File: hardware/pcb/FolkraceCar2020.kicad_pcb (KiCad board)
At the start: 2 copper layers, 3 parts, among them J2 Jetson Nano Header, U1 TPS25940x-Q1, U2 OKL-T_6-W12N-C

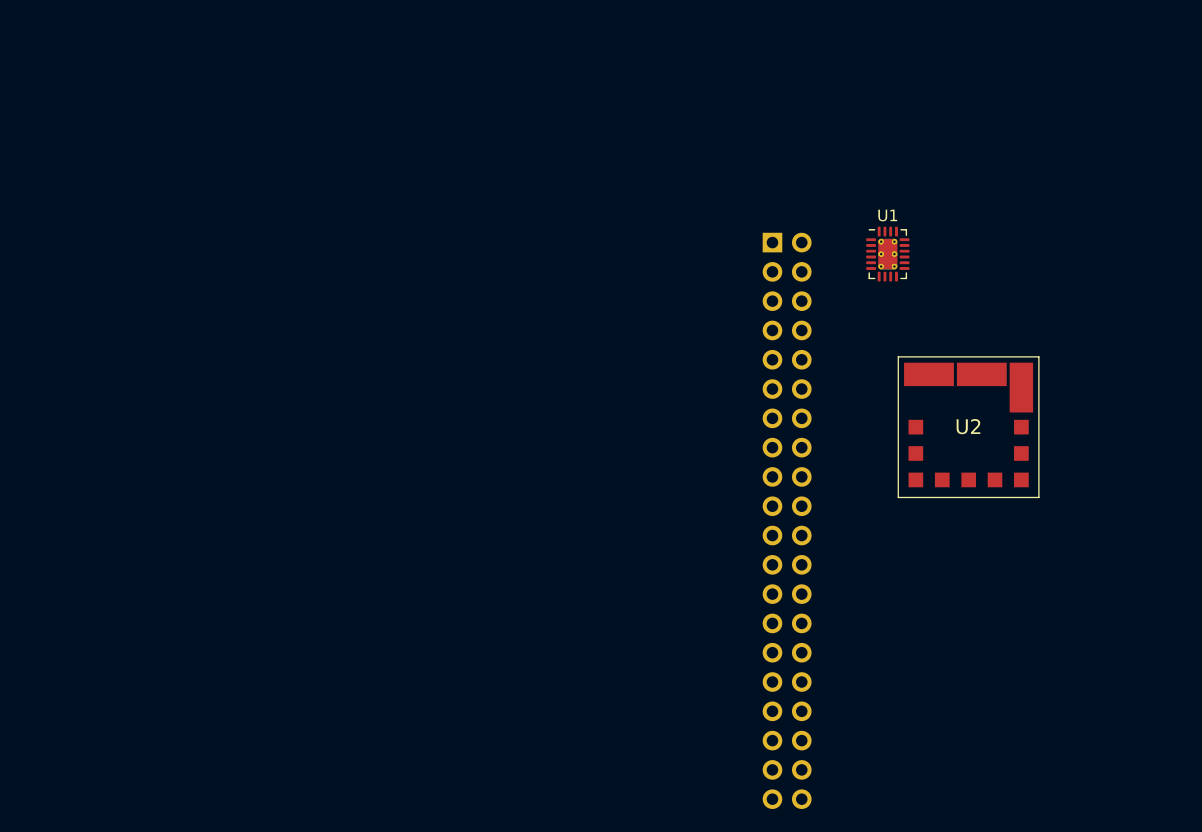
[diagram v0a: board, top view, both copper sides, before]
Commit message: Outline added to pcb layout
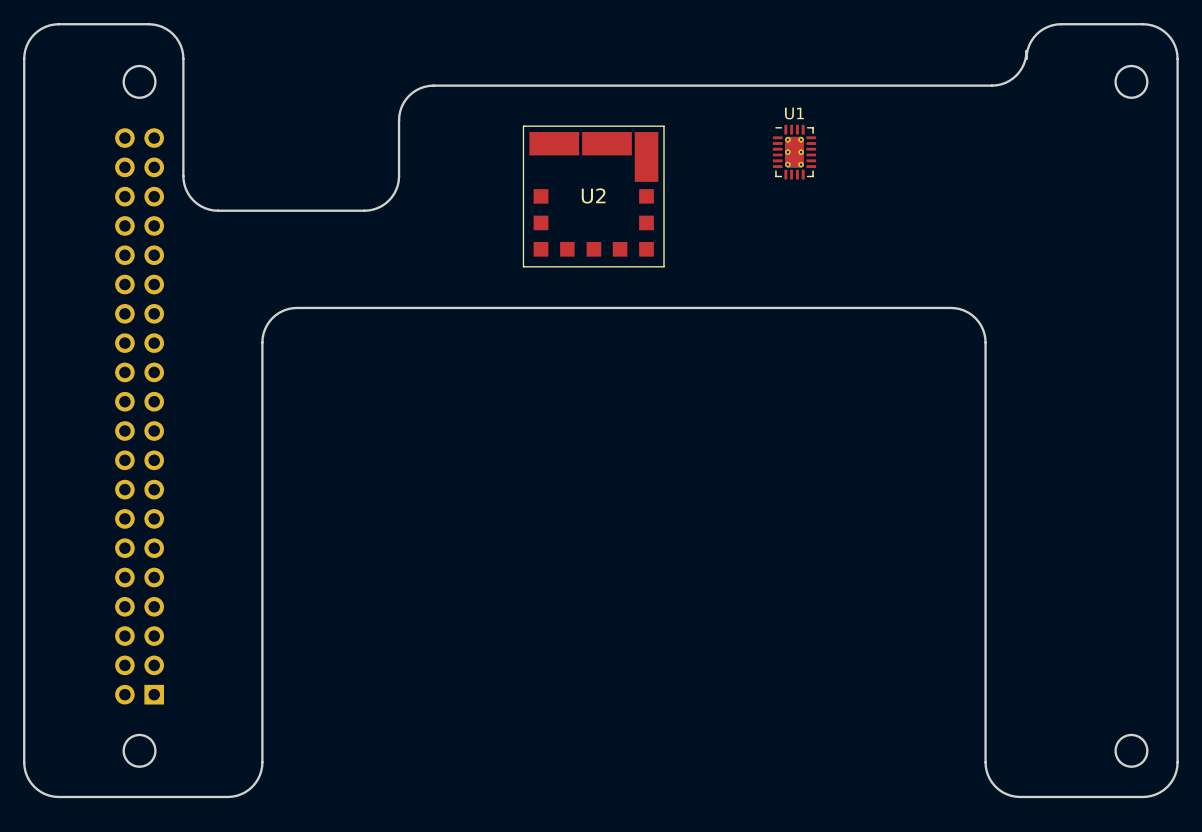
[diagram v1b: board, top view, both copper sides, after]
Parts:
- moved J2 66.4 mm to (86.4, 134.2), turned to 0 degrees
- moved U2 38.2 mm to (124.5, 91.0)
- moved U1 12.0 mm to (141.9, 87.2)
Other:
- board outline added: 100 x 67 mm

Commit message: updated schematic
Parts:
- added D1: LED RED, LED_SMD:LED_0603_1608Metric, F.Cu at (162.5, 87.0)
- added D2: LED GREEN, LED_SMD:LED_0603_1608Metric, F.Cu at (157.5, 92.2)
- added R1: R, Resistor_SMD:R_0603_1608Metric, F.Cu at (150.5, 96.8)
- added R2: R, Resistor_SMD:R_0603_1608Metric, F.Cu at (162.5, 89.5)
- added R3: R, Resistor_SMD:R_0603_1608Metric, F.Cu at (154.5, 96.8)
- added R4: R, Resistor_SMD:R_0603_1608Metric, F.Cu at (166.5, 87.0)
- added R5: R, Resistor_SMD:R_0603_1608Metric, F.Cu at (161.5, 92.1)
- added R6: R, Resistor_SMD:R_0603_1608Metric, F.Cu at (166.5, 89.5)
- added R8: R, Resistor_SMD:R_0603_1608Metric, F.Cu at (158.5, 94.7)
- added SW1: SPST, Button_Switch_SMD:SW_DIP_SPSTx01_Slide_Omron_A6S-110x_W8.9mm_P2.54mm, F.Cu at (154.5, 88.3)
- added U3: ADS1115IDGS, Package_SO:TSSOP-10_3x3mm_P0.5mm, F.Cu at (152.0, 93.2)
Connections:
- U1 pad 16: Net-(U1-Pad16) -> GND
- U1 pad 2: Net-(U1-Pad2) -> Net-(R8-Pad1)
- U1 pad 21: Net-(U1-Pad21) -> GND
- U1 pad 3: Net-(U1-Pad3) -> VBUS
- U1 pad 4: Net-(U1-Pad4) -> VBUS
- U1 pad 5: Net-(U1-Pad5) -> VBUS
- U1 pad 6: Net-(U1-Pad6) -> VBUS
- U1 pad 7: Net-(U1-Pad7) -> VBUS
- U1 pad 8: Net-(U1-Pad8) -> VBUS
- U2 pad 1: Net-(U2-Pad1) -> Net-(R8-Pad1)
- U2 pad 2: Net-(U2-Pad2) -> VBUS

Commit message: added todo in schematic
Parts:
- added D3: LED GREEN, LED_SMD:LED_0603_1608Metric, F.Cu at (127.4, 74.3)
- added J3: Conn_01x03_Male, Connector_JST:JST_PH_B3B-PH-K_1x03_P2.00mm_Vertical, F.Cu at (110.5, 75.7)
- added J4: Conn_01x02_Male, Connector_JST:JST_PH_B2B-PH-K_1x02_P2.00mm_Vertical, F.Cu at (120.4, 75.7)
- added Q1: BSS138, Package_TO_SOT_SMD:SOT-23, F.Cu at (109.7, 81.8)
- added Q2: DMN10H220L, Package_TO_SOT_SMD:SOT-23, F.Cu at (114.2, 81.8)
- added R10: R, Resistor_SMD:R_0603_1608Metric, F.Cu at (118.4, 83.3)
- added R11: R, Resistor_SMD:R_0603_1608Metric, F.Cu at (127.4, 79.4)
- added R12: R, Resistor_SMD:R_0603_1608Metric, F.Cu at (122.4, 83.3)
- added R7: R, Resistor_SMD:R_0603_1608Metric, F.Cu at (127.4, 76.8)
- added R9: 1.3k, Resistor_SMD:R_0603_1608Metric, F.Cu at (122.4, 80.8)
- R5: value R -> 0
- moved R5 44.6 mm to (118.4, 80.8)
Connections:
- R5 pad 1: Net-(R4-Pad1) -> Net-(R5-Pad1)
- R5 pad 2: GND -> Net-(Q1-Pad3)
- R8 pad 1: Net-(R8-Pad1) -> Net-(Q1-Pad1)
- U1 pad 19: Net-(R7-Pad1) -> /IMON
- U1 pad 2: Net-(R8-Pad1) -> Net-(Q1-Pad1)
- U2 pad 1: Net-(R8-Pad1) -> Net-(R5-Pad1)
- U2 pad 3: Net-(U2-Pad3) -> GND
- U2 pad 4: Net-(U2-Pad4) -> +5V
- U2 pad 5: Net-(U2-Pad5) -> +5V
- U2 pad 7: Net-(U2-Pad7) -> GND
- U3 pad 3: Net-(U3-Pad3) -> GND
- U3 pad 4: Net-(U3-Pad4) -> /VMON
- U3 pad 5: Net-(U3-Pad5) -> /IMON

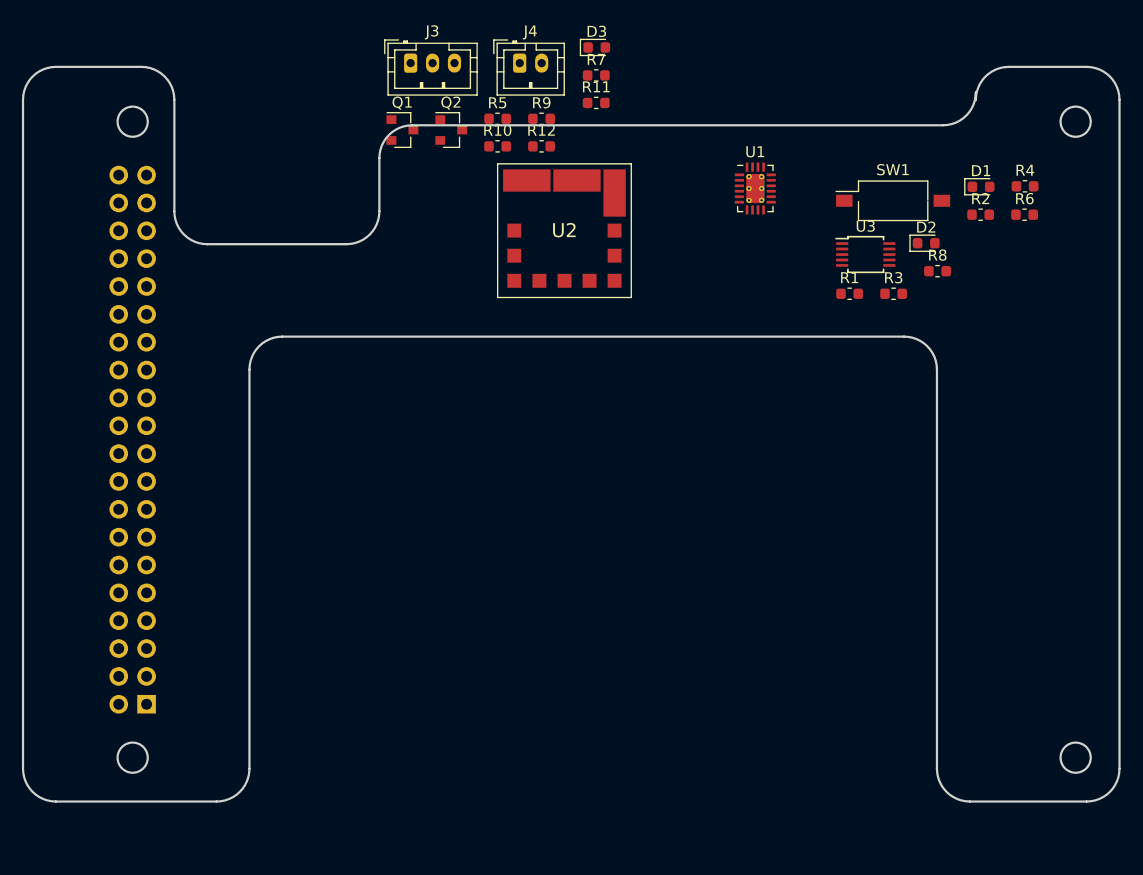
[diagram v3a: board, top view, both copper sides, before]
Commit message: added new outline and RP connector
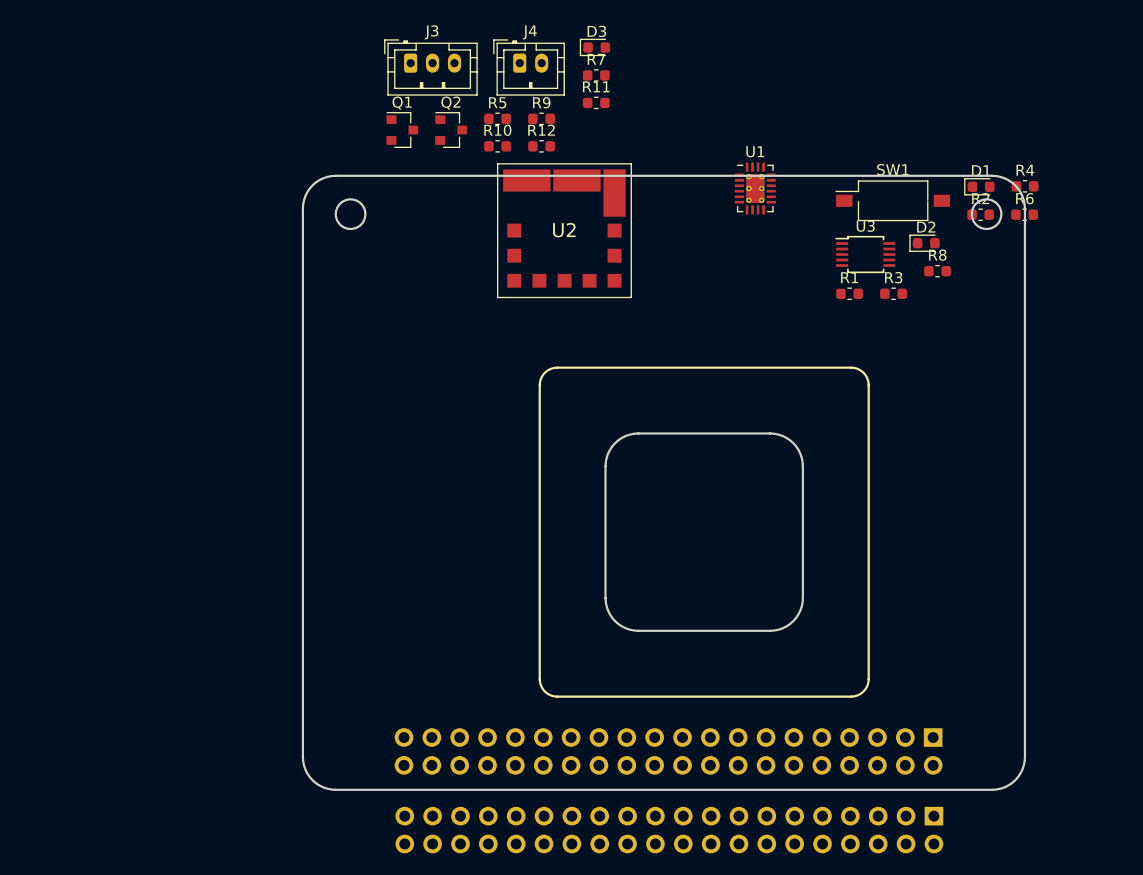
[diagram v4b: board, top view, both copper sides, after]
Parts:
- added J5: Raspberry_Pi_2_3, Connector_PinSocket_2.54mm:PinSocket_2x20_P2.54mm_Vertical, B.Cu at (158.2, 144.4)
- moved J2 71.8 mm to (158.1, 137.2), turned to 90 degrees
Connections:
- J2 pad 10: /UART_2_RX -> (no net)
- J2 pad 11: /UART_2_RTS -> (no net)
- J2 pad 12: /I2S_4_SCLK -> (no net)
- J2 pad 13: /SPI_2_SCK -> (no net)
- J2 pad 15: /LCD_TE -> (no net)
- J2 pad 16: /SPI_2_CS1 -> (no net)
- J2 pad 18: /SPI_2_CS0 -> (no net)
- J2 pad 19: /SPI_1_MOSI -> (no net)
- J2 pad 21: /SPI_1_MISO -> (no net)
- J2 pad 22: /SPI_2_MISO -> (no net)
- J2 pad 23: /SPI_1_SCK -> (no net)
- J2 pad 24: /SPI_1_CS0 -> (no net)
- J2 pad 26: /SPI_1_CS1 -> (no net)
- J2 pad 27: /I2C_1_SDA -> (no net)
- J2 pad 28: /I2C_1_SCL -> (no net)
- J2 pad 29: /CAM_AF_EN -> (no net)
- J2 pad 3: /I2C_2SDA -> (no net)
- J2 pad 31: /GPIO_PZ0 -> (no net)
- J2 pad 32: /LCD_BL_PWM -> (no net)
- J2 pad 33: /GPIO_PE6 -> (no net)
- J2 pad 35: /I2S_4_LRCK -> (no net)
- J2 pad 36: /UART_2_CTS -> (no net)
- J2 pad 37: /SPI_2_MOSI -> (no net)
- J2 pad 38: /I2S_4_SDIN -> (no net)
- J2 pad 40: /I2S_4_SDOUT -> (no net)
- J2 pad 5: /I2C_2_SCL -> (no net)
- J2 pad 7: /AUDIO_MCLK -> (no net)
- J2 pad 8: /UART_2_TX -> (no net)
- J3 pad 2: /SERVO_PWM -> (no net)
- Q2 pad 1: /FAN_CTRL -> (no net)
- U1 pad 1: Net-(U1-Pad1) -> (no net)
- U1 pad 18: Net-(C3-Pad1) -> (no net)
- U2 pad 11: Net-(U2-Pad11) -> (no net)
- U2 pad 12: Net-(U2-Pad12) -> (no net)
- U2 pad 8: Net-(U2-Pad8) -> (no net)
- U2 pad 9: Net-(U2-Pad9) -> (no net)
- U3 pad 1: Net-(U3-Pad1) -> (no net)
- U3 pad 10: Net-(U3-Pad10) -> (no net)
- U3 pad 2: Net-(U3-Pad2) -> (no net)
- U3 pad 6: Net-(U3-Pad6) -> (no net)
- U3 pad 7: Net-(U3-Pad7) -> (no net)
- U3 pad 8: Net-(C4-Pad1) -> (no net)
- U3 pad 9: Net-(U3-Pad9) -> (no net)
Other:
- board size 100 x 67 mm -> 65.8 x 56 mm

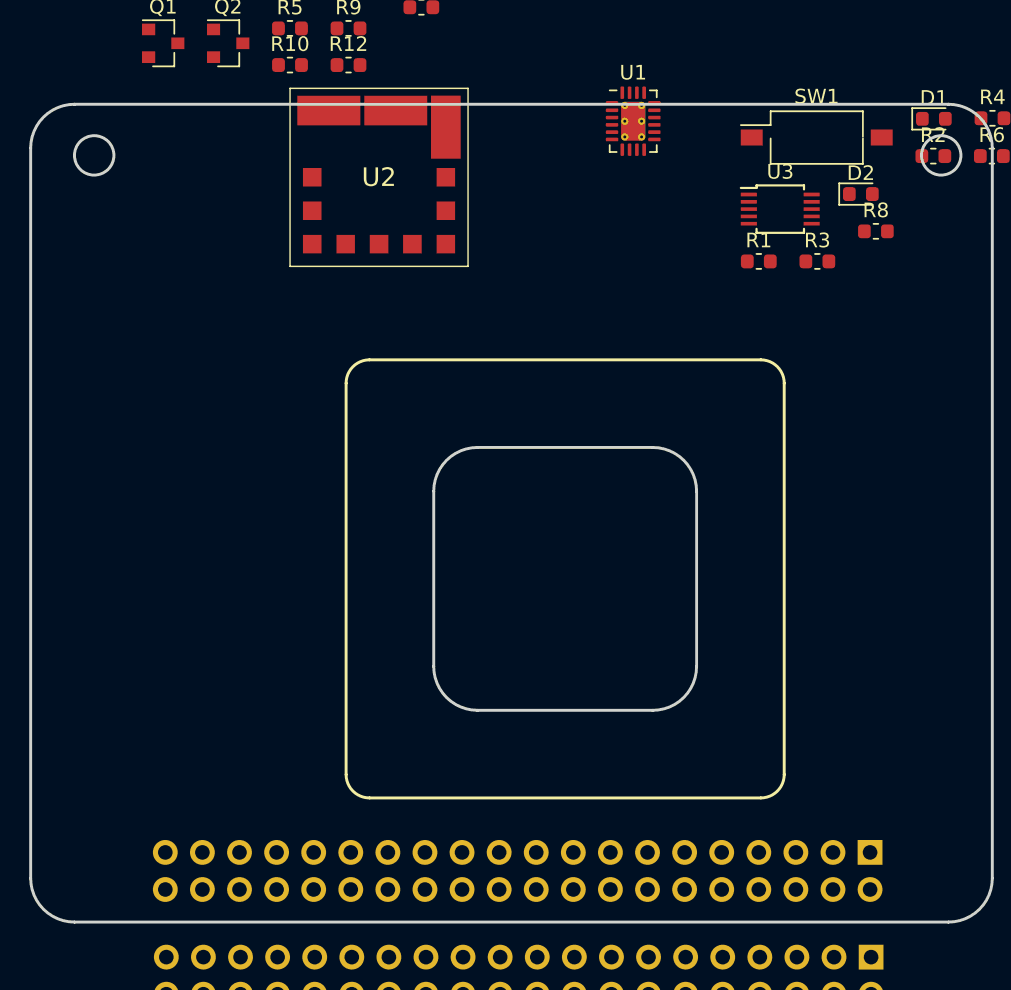
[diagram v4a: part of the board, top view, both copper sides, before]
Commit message: added symbol, footprint and 3d model for DRV8874
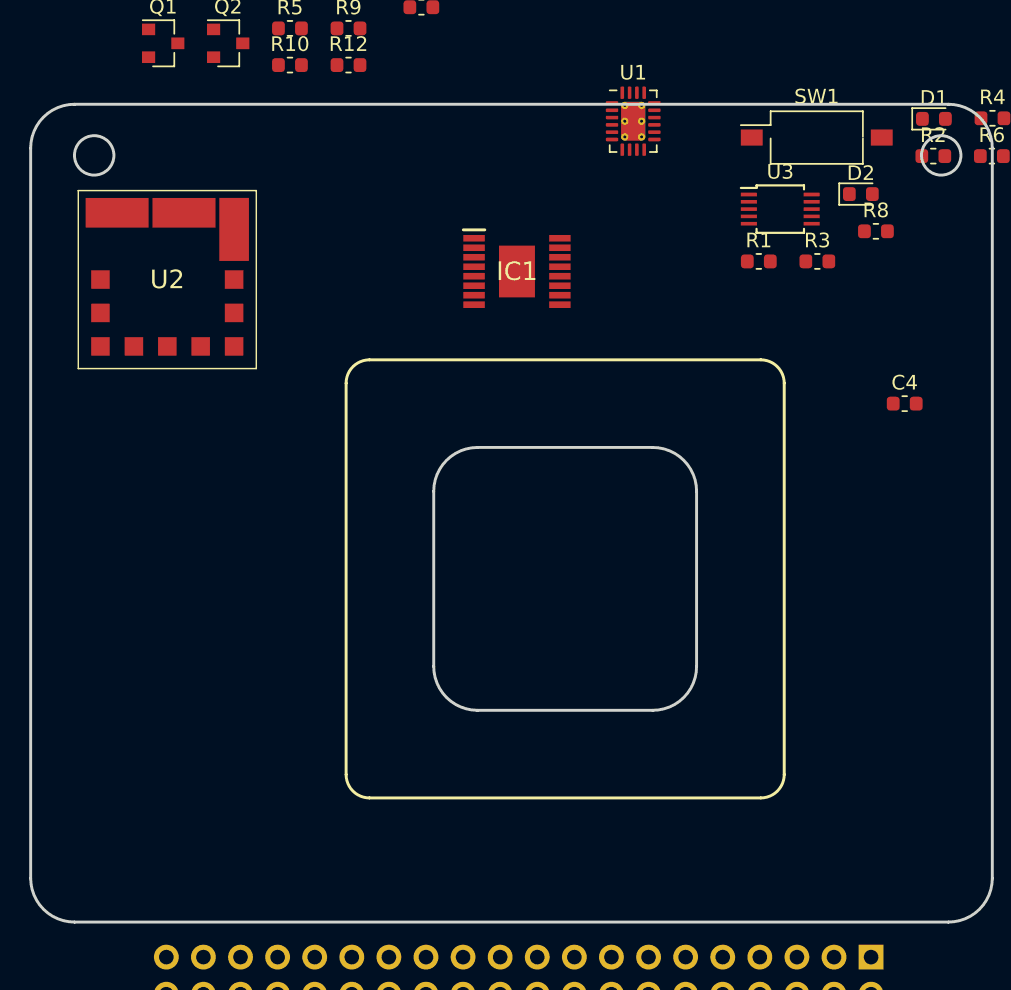
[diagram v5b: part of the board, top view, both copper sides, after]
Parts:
- removed J2: Jetson Nano Header, Connector_PinSocket_2.54mm:PinSocket_2x20_P2.54mm_Vertical
- added C4: C, Capacitor_SMD:C_0603_1608Metric, F.Cu at (160.5, 106.5)
- added IC1: DRV8874PWPR, DCDC:SOP65P640X120-17N, F.Cu at (134.0, 97.5)
- J5: value Raspberry_Pi_2_3 -> Raspberry_Pi
- moved U2 16.1 mm to (110.0, 98.0)
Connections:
- J3 pad 2: (no net) -> /SERVO_PWM
- J5 pad 1: (no net) -> +3V3
- J5 pad 10: (no net) -> Net-(J5-Pad10)
- J5 pad 11: (no net) -> Net-(J5-Pad11)
- J5 pad 12: (no net) -> Net-(J5-Pad12)
- J5 pad 13: (no net) -> Net-(J5-Pad13)
- J5 pad 14: (no net) -> GND
- J5 pad 15: (no net) -> Net-(J5-Pad15)
- J5 pad 16: (no net) -> Net-(J5-Pad16)
- J5 pad 17: (no net) -> +3V3
- J5 pad 18: (no net) -> Net-(J5-Pad18)
- J5 pad 19: (no net) -> Net-(J5-Pad19)
- J5 pad 2: (no net) -> +5V
- J5 pad 20: (no net) -> GND
- J5 pad 21: (no net) -> Net-(J5-Pad21)
- J5 pad 22: (no net) -> Net-(J5-Pad22)
- J5 pad 23: (no net) -> Net-(J5-Pad23)
- J5 pad 24: (no net) -> Net-(J5-Pad24)
- J5 pad 25: (no net) -> GND
- J5 pad 26: (no net) -> Net-(J5-Pad26)
- J5 pad 27: (no net) -> Net-(J5-Pad27)
- J5 pad 28: (no net) -> Net-(J5-Pad28)
- J5 pad 29: (no net) -> Net-(J5-Pad29)
- J5 pad 3: (no net) -> Net-(J5-Pad3)
- J5 pad 30: (no net) -> GND
- J5 pad 31: (no net) -> Net-(J5-Pad31)
- J5 pad 32: (no net) -> Net-(J5-Pad32)
- J5 pad 33: (no net) -> Net-(J5-Pad33)
- J5 pad 34: (no net) -> GND
- J5 pad 35: (no net) -> Net-(J5-Pad35)
- J5 pad 36: (no net) -> Net-(J5-Pad36)
- J5 pad 37: (no net) -> Net-(J5-Pad37)
- J5 pad 38: (no net) -> Net-(J5-Pad38)
- J5 pad 39: (no net) -> GND
- J5 pad 4: (no net) -> +5V
- J5 pad 40: (no net) -> Net-(J5-Pad40)
- J5 pad 5: (no net) -> Net-(J5-Pad5)
- J5 pad 6: (no net) -> GND
- J5 pad 7: (no net) -> Net-(J5-Pad7)
- J5 pad 8: (no net) -> Net-(J5-Pad8)
- J5 pad 9: (no net) -> GND
- Q2 pad 1: (no net) -> /FAN_CTRL
- U1 pad 1: (no net) -> Net-(U1-Pad1)
- U1 pad 18: (no net) -> Net-(C3-Pad1)
- U2 pad 11: (no net) -> Net-(U2-Pad11)
- U2 pad 12: (no net) -> Net-(U2-Pad12)
- U2 pad 8: (no net) -> Net-(U2-Pad8)
- U2 pad 9: (no net) -> Net-(U2-Pad9)
- U3 pad 1: (no net) -> Net-(U3-Pad1)
- U3 pad 10: (no net) -> Net-(U3-Pad10)
- U3 pad 2: (no net) -> Net-(U3-Pad2)
- U3 pad 6: (no net) -> Net-(U3-Pad6)
- U3 pad 7: (no net) -> Net-(U3-Pad7)
- U3 pad 8: (no net) -> +3V3
- U3 pad 9: (no net) -> Net-(U3-Pad9)
